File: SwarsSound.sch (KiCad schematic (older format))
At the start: 162 parts, among them P1 Main_Connector, P2 aud_con, P3 edge_con, Q1 2N3906f, Q2 2N3906f, Q3 2N3904, Q4 2N3904

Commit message: Verified spacing and added some traces
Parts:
- C13, C14: footprint Star_Wars_Vector_PCB:LargeCap -> Star_Wars_Vector_PCB:CapElec3
- C15, C47, C53: footprint Star_Wars_Vector_PCB:LargeCap -> Star_Wars_Vector_PCB:CapElec2
- C51, C52: footprint Star_Wars_Main_PCB:Cap1 -> Star_Wars_Vector_PCB:CapElec2
- Q3, Q4: footprint Package_TO_SOT_THT:TO-92_Inline -> Star_Wars_Vector_PCB:GenericTrans
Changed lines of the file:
@@
 F 0 "C51" V 19825 11675 50  0000 C CNN
 F 1 "0.47" V 19750 11675 50  0000 C CNN
-F 2 "Star_Wars_Main_PCB:Cap1" H 19663 11525 50  0001 C CNN
+F 2 "Star_Wars_Vector_PCB:CapElec2" H 19663 11525 50  0001 C CNN
 F 3 "~" H 19625 11675 50  0001 C CNN
 	1    19625 11675
@@
 F 0 "C52" H 21250 12700 50  0000 C CNN
 F 1 "10" H 21250 12775 50  0000 C CNN
-F 2 "Star_Wars_Main_PCB:Cap1" H 21488 12575 50  0001 C CNN
+F 2 "Star_Wars_Vector_PCB:CapElec2" H 21488 12575 50  0001 C CNN
 F 3 "~" H 21450 12725 50  0001 C CNN
 	1    21450 12725
@@
 F 0 "C53" V 22125 10925 50  0000 C CNN
 F 1 "100" V 22050 10925 50  0000 C CNN
-F 2 "Star_Wars_Vector_PCB:LargeCap" H 21963 10775 50  0001 C CNN
+F 2 "Star_Wars_Vector_PCB:CapElec2" H 21963 10775 50  0001 C CNN
 F 3 "~" H 21925 10925 50  0001 C CNN
 	1    21925 10925
@@
 F 0 "Q4" H 23440 16071 50  0000 L CNN
 F 1 "2N3904" H 23440 15980 50  0000 L CNN
-F 2 "Package_TO_SOT_THT:TO-92_Inline" H 23450 15950 50  0001 L CIN
+F 2 "Star_Wars_Vector_PCB:GenericTrans" H 23450 15950 50  0001 L CIN
 F 3 "https://www.onsemi.com/pub/Collateral/2N3903-D.PDF" H 23250 16025 50  0001 L CNN
 	1    23250 16025
@@
 F 0 "C47" H 24100 15075 50  0000 C CNN
 F 1 "100" H 24100 15150 50  0000 C CNN
-F 2 "Star_Wars_Vector_PCB:LargeCap" H 23963 14950 50  0001 C CNN
+F 2 "Star_Wars_Vector_PCB:CapElec2" H 23963 14950 50  0001 C CNN
 F 3 "~" H 23925 15100 50  0001 C CNN
 	1    23925 15100
@@
 F 0 "Q3" H 13950 17300 50  0000 L CNN
 F 1 "2N3904" H 13950 17225 50  0000 L CNN
-F 2 "Package_TO_SOT_THT:TO-92_Inline" H 13950 17175 50  0001 L CIN
+F 2 "Star_Wars_Vector_PCB:GenericTrans" H 13950 17175 50  0001 L CIN
 F 3 "https://www.onsemi.com/pub/Collateral/2N3903-D.PDF" H 13750 17250 50  0001 L CNN
 	1    13750 17250
@@
 F 0 "C13" H 28600 13550 50  0000 C CNN
 F 1 "100" H 28600 13625 50  0000 C CNN
-F 2 "Star_Wars_Vector_PCB:LargeCap" H 28463 13425 50  0001 C CNN
+F 2 "Star_Wars_Vector_PCB:CapElec3" H 28463 13425 50  0001 C CNN
 F 3 "~" H 28425 13575 50  0001 C CNN
 	1    28425 13575
@@
 F 0 "C14" H 28600 14650 50  0000 C CNN
 F 1 "100" H 28600 14725 50  0000 C CNN
-F 2 "Star_Wars_Vector_PCB:LargeCap" H 28463 14525 50  0001 C CNN
+F 2 "Star_Wars_Vector_PCB:CapElec3" H 28463 14525 50  0001 C CNN
 F 3 "~" H 28425 14675 50  0001 C CNN
 	1    28425 14675
@@
 F 0 "C15" H 28625 15575 50  0000 C CNN
 F 1 "100" H 28625 15650 50  0000 C CNN
-F 2 "Star_Wars_Vector_PCB:LargeCap" H 28488 15450 50  0001 C CNN
+F 2 "Star_Wars_Vector_PCB:CapElec2" H 28488 15450 50  0001 C CNN
 F 3 "~" H 28450 15600 50  0001 C CNN
 	1    28450 15600

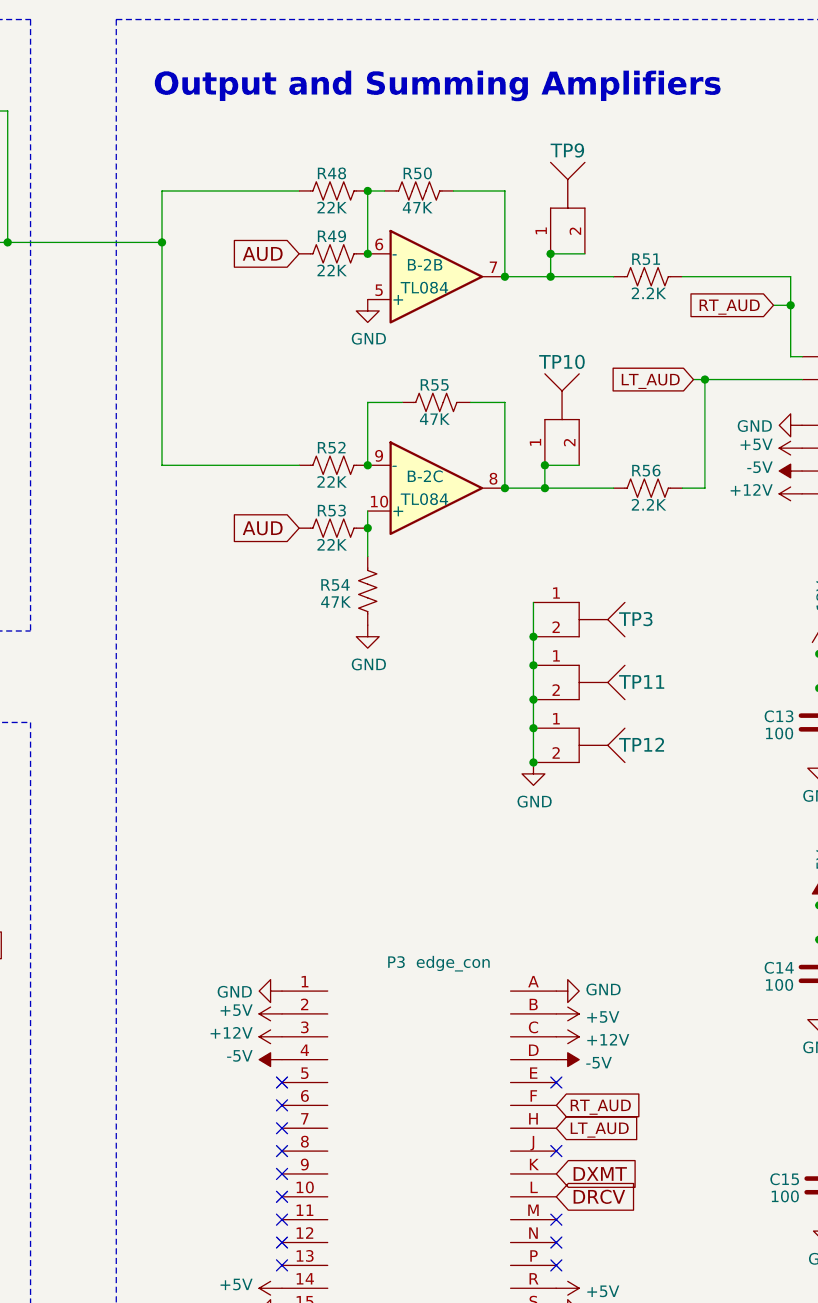
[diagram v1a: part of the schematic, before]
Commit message: Modified some traces
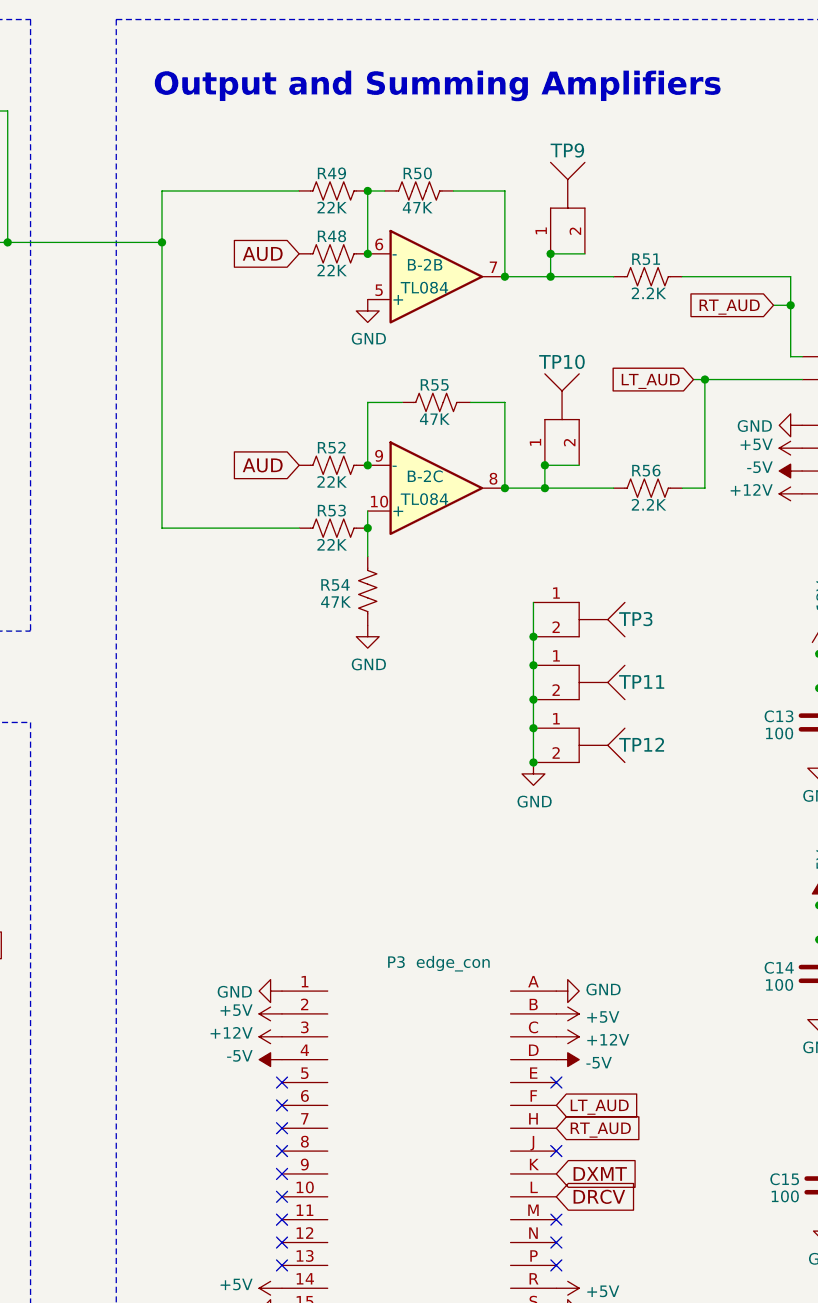
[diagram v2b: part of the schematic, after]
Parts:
- renumbered R49 to R48, R48 to R49
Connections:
- net AUD: now also R52.2; no longer R53.2
- net LT_AUD: now also P3.F; no longer P3.H
- net RT_AUD: now also P3.H; no longer P3.F
- net at B-2.1, B-2.2 (-), C56.2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: now also R53.2; no longer R52.2
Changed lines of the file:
@@
 Text GLabel 26150 11525 0    60   Input ~ 0
 AUD
-Text GLabel 26150 12725 0    60   Input ~ 0
+Text GLabel 26150 12450 0    60   Input ~ 0
 AUD
 $Comp
-L Device:R_US R49
+L Device:R_US R48
 U 1 1 6149A659
 P 26300 11525
-F 0 "R49" V 26225 11450 50  0000 L CNN
+F 0 "R48" V 26225 11450 50  0000 L CNN
 F 1 "22K" V 26375 11450 50  0000 L CNN
 F 2 "Star_Wars_Vector_PCB:GenericComp" V 26340 11515 50  0001 C CNN
@@
 $EndComp
 $Comp
-L Device:R_US R48
+L Device:R_US R49
 U 1 1 6149B132
 P 26300 11250
-F 0 "R48" V 26225 11175 50  0000 L CNN
+F 0 "R49" V 26225 11175 50  0000 L CNN
 F 1 "22K" V 26375 11175 50  0000 L CNN
 F 2 "Star_Wars_Vector_PCB:GenericComp" V 26340 11240 50  0001 C CNN
@@
 Wire Wire Line
 	24875 11475 24775 11475
-Wire Wire Line
-	25550 12450 26150 12450
 $Comp
 L Device:R_US R50
@@
 	25550 11250 25550 11475
 Connection ~ 25550 11475
-Wire Wire Line
-	25550 11475 25550 12450
 Connection ~ 24875 11475
 $Comp
@@
 Wire Wire Line
 	28300 11750 28300 11975
-Text GLabel 27275 15250 2    50   Input ~ 0
-RT_AUD
 Text GLabel 27275 15350 2    50   Input ~ 0
+RT_AUD
+Text GLabel 27275 15250 2    50   Input ~ 0
 LT_AUD
 NoConn ~ 26075 15950
@@
 	0    -1   -1   0
 $EndComp
+Wire Wire Line
+	26150 12725 25550 12725
+Wire Wire Line
+	25550 11475 25550 12725
 $EndSCHEMATC

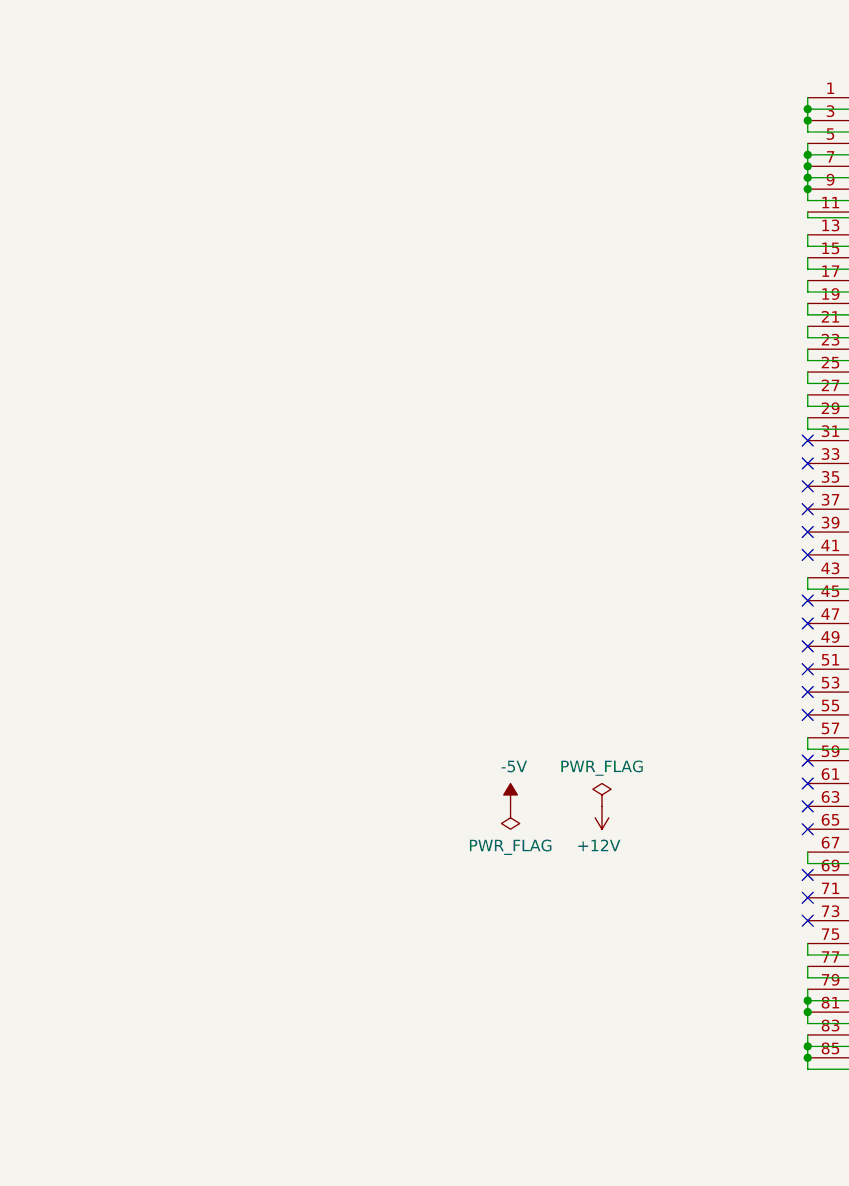
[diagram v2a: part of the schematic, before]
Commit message: Completed the back of the PCB
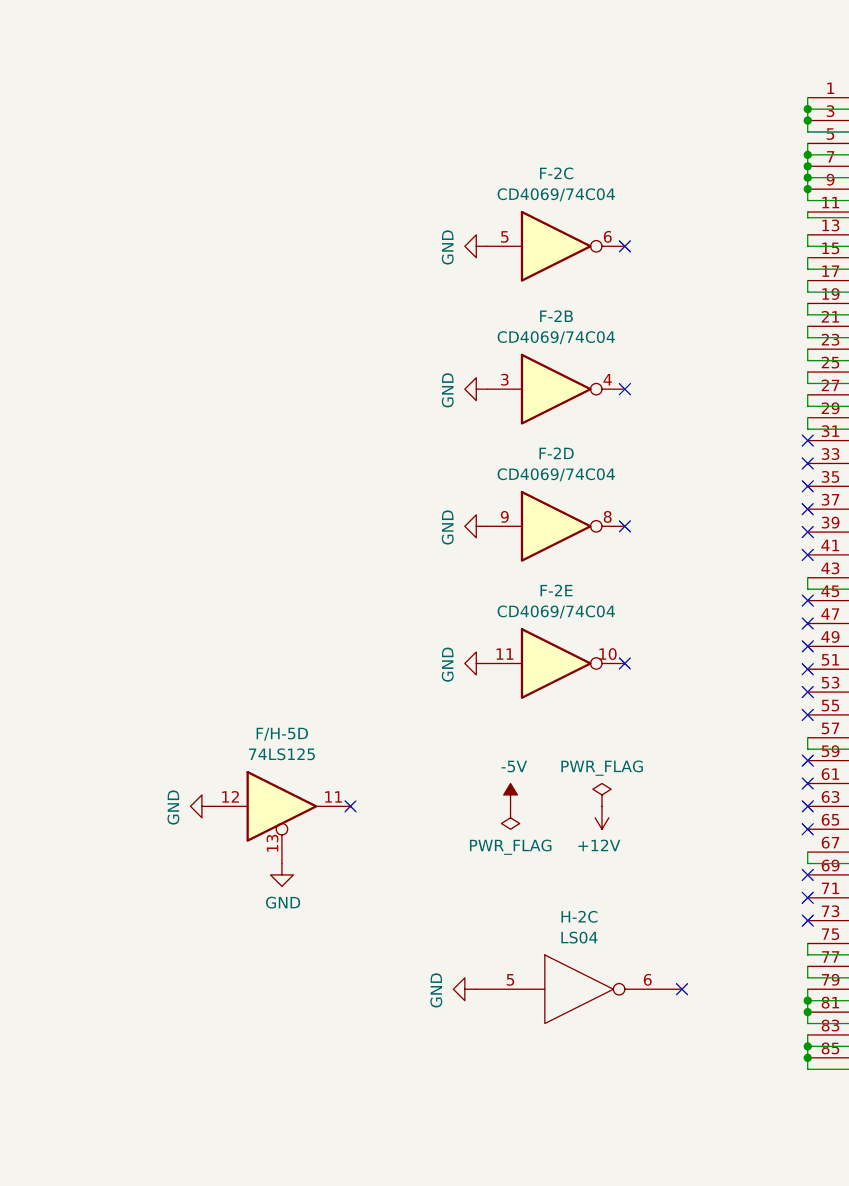
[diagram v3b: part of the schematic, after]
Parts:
- added unit 5 of F-2
- added unit 4 of F-2
- added unit 2 of F-2
- added unit 3 of F-2
- added unit 4 of F/H-5
- added unit 3 of H-2
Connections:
- net GND: now also F-2.11, F-2.3, F-2.5, F-2.9, F/H-5.12, F/H-5.13, H-2.5
- no-connect marks 101 -> 107
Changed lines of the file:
@@
 Wire Wire Line
 	25550 11475 25550 12725
+$Comp
+L Asteroids:LS04 H-2
+U 3 1 60FC6B94
+P 29000 21000
+F 0 "H-2" H 29000 21315 50  0000 C CNN
+F 1 "LS04" H 29000 21224 50  0000 C CNN
+F 2 "" H 29000 21000 50  0001 C CNN
+F 3 "" H 29000 21000 50  0001 C CNN
+	3    29000 21000
+	1    0    0    -1
+$EndComp
+NoConn ~ 29450 21000
+$Comp
+L power:GND #PWR0253
+U 1 1 6101B723
+P 28550 21000
+F 0 "#PWR0253" H 28550 20750 50  0001 C CNN
+F 1 "GND" H 28555 20827 50  0000 C CNN
+F 2 "" H 28550 21000 50  0001 C CNN
+F 3 "" H 28550 21000 50  0001 C CNN
+	1    28550 21000
+	0    1    1    0
+$EndComp
+$Comp
+L SwarsSound-rescue:4069-4xxx F-2
+U 5 1 6118642A
+P 28900 19575
+F 0 "F-2" H 28900 19892 50  0000 C CNN
+F 1 "CD4069/74C04" H 28900 19801 50  0000 C CNN
+F 2 "" H 28900 19575 50  0001 C CNN
+F 3 "" H 28900 19575 50  0001 C CNN
+	5    28900 19575
+	1    0    0    -1
+$EndComp
+$Comp
+L power:GND #PWR0254
+U 1 1 6119DC0D
+P 28600 19575
+F 0 "#PWR0254" H 28600 19325 50  0001 C CNN
+F 1 "GND" H 28605 19402 50  0000 C CNN
+F 2 "" H 28600 19575 50  0001 C CNN
+F 3 "" H 28600 19575 50  0001 C CNN
+	1    28600 19575
+	0    1    1    0
+$EndComp
+NoConn ~ 29200 19575
+$Comp
+L SwarsSound-rescue:4069-4xxx F-2
+U 4 1 611EEEC4
+P 28900 18975
+F 0 "F-2" H 28900 19292 50  0000 C CNN
+F 1 "CD4069/74C04" H 28900 19201 50  0000 C CNN
+F 2 "" H 28900 18975 50  0001 C CNN
+F 3 "" H 28900 18975 50  0001 C CNN
+	4    28900 18975
+	1    0    0    -1
+$EndComp
+$Comp
+L power:GND #PWR0255
+U 1 1 611EF462
+P 28600 18975
+F 0 "#PWR0255" H 28600 18725 50  0001 C CNN
+F 1 "GND" H 28605 18802 50  0000 C CNN
+F 2 "" H 28600 18975 50  0001 C CNN
+F 3 "" H 28600 18975 50  0001 C CNN
+	1    28600 18975
+	0    1    1    0
+$EndComp
+NoConn ~ 29200 18975
+$Comp
+L SwarsSound-rescue:4069-4xxx F-2
+U 2 1 61240F25
+P 28900 18375
+F 0 "F-2" H 28900 18692 50  0000 C CNN
+F 1 "CD4069/74C04" H 28900 18601 50  0000 C CNN
+F 2 "" H 28900 18375 50  0001 C CNN
+F 3 "" H 28900 18375 50  0001 C CNN
+	2    28900 18375
+	1    0    0    -1
+$EndComp
+$Comp
+L power:GND #PWR0256
+U 1 1 6124193C
+P 28600 18375
+F 0 "#PWR0256" H 28600 18125 50  0001 C CNN
+F 1 "GND" H 28605 18202 50  0000 C CNN
+F 2 "" H 28600 18375 50  0001 C CNN
+F 3 "" H 28600 18375 50  0001 C CNN
+	1    28600 18375
+	0    1    1    0
+$EndComp
+NoConn ~ 29200 18375
+$Comp
+L 74xx:74LS125 F/H-5
+U 4 1 61297A63
+P 27700 20200
+F 0 "F/H-5" H 27700 20517 50  0000 C CNN
+F 1 "74LS125" H 27700 20426 50  0000 C CNN
+F 2 "" H 27700 20200 50  0001 C CNN
+F 3 "http://www.ti.com/lit/gpn/sn74LS125" H 27700 20200 50  0001 C CNN
+	4    27700 20200
+	1    0    0    -1
+$EndComp
+$Comp
+L power:GND #PWR0257
+U 1 1 612A2383
+P 27400 20200
+F 0 "#PWR0257" H 27400 19950 50  0001 C CNN
+F 1 "GND" H 27405 20027 50  0000 C CNN
+F 2 "" H 27400 20200 50  0001 C CNN
+F 3 "" H 27400 20200 50  0001 C CNN
+	1    27400 20200
+	0    1    1    0
+$EndComp
+$Comp
+L power:GND #PWR0258
+U 1 1 612A282A
+P 27700 20450
+F 0 "#PWR0258" H 27700 20200 50  0001 C CNN
+F 1 "GND" H 27705 20277 50  0000 C CNN
+F 2 "" H 27700 20450 50  0001 C CNN
+F 3 "" H 27700 20450 50  0001 C CNN
+	1    27700 20450
+	1    0    0    -1
+$EndComp
+NoConn ~ 28000 20200
+$Comp
+L SwarsSound-rescue:4069-4xxx F-2
+U 3 1 61300046
+P 28900 17750
+F 0 "F-2" H 28900 18067 50  0000 C CNN
+F 1 "CD4069/74C04" H 28900 17976 50  0000 C CNN
+F 2 "" H 28900 17750 50  0001 C CNN
+F 3 "" H 28900 17750 50  0001 C CNN
+	3    28900 17750
+	1    0    0    -1
+$EndComp
+$Comp
+L power:GND #PWR?
+U 1 1 613014FD
+P 28600 17750
+F 0 "#PWR?" H 28600 17500 50  0001 C CNN
+F 1 "GND" H 28605 17577 50  0000 C CNN
+F 2 "" H 28600 17750 50  0001 C CNN
+F 3 "" H 28600 17750 50  0001 C CNN
+	1    28600 17750
+	0    1    1    0
+$EndComp
+NoConn ~ 29200 17750
 $EndSCHEMATC

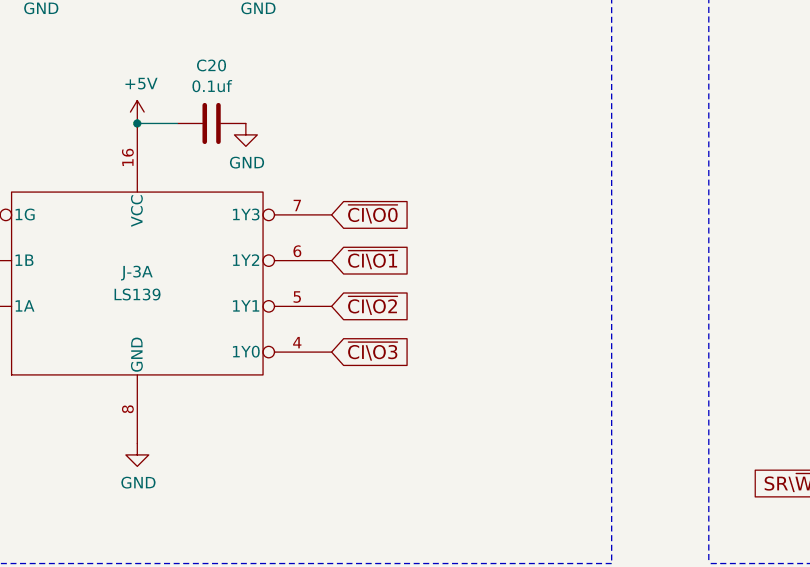
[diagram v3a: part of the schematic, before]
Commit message: Finished top layer traces
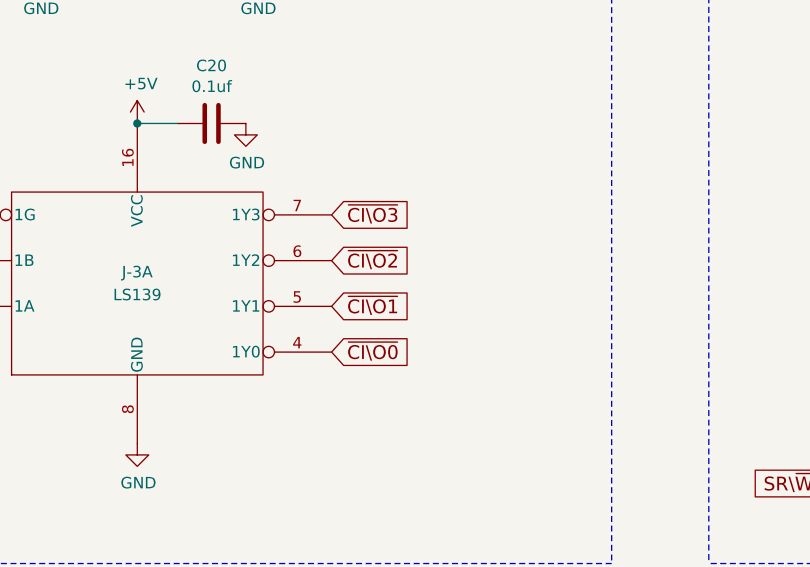
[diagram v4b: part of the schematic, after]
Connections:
- net ~CI\O0: now also J-3.4 (1Y0); no longer J-3.7 (1Y3)
- net ~CI\O1: now also J-3.5 (1Y1); no longer J-3.6 (1Y2)
- net ~CI\O2: now also J-3.6 (1Y2); no longer J-3.5 (1Y1)
- net ~CI\O3: now also J-3.7 (1Y3); no longer J-3.4 (1Y0)
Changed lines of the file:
@@
 Text GLabel 17250 2350 0    60   Input ~ 0
 SA13
+Text GLabel 19125 7400 2    60   Input ~ 0
+~CI\O2
 Text GLabel 19125 7600 2    60   Input ~ 0
-~CI\O2
-Text GLabel 19125 7400 2    60   Input ~ 0
 ~CI\O1
-Text GLabel 19125 7200 2    60   Input ~ 0
+Text GLabel 19125 7800 2    60   Input ~ 0
 ~CI\O0
 Text GLabel 18950 3950 2    60   Input ~ 0
@@
 Text GLabel 18950 2150 2    60   Input ~ 0
 ~SROM0
-Text GLabel 19125 7800 2    60   Input ~ 0
+Text GLabel 19125 7200 2    60   Input ~ 0
 ~CI\O3
 Wire Wire Line
